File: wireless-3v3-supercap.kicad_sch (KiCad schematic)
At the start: 8 parts

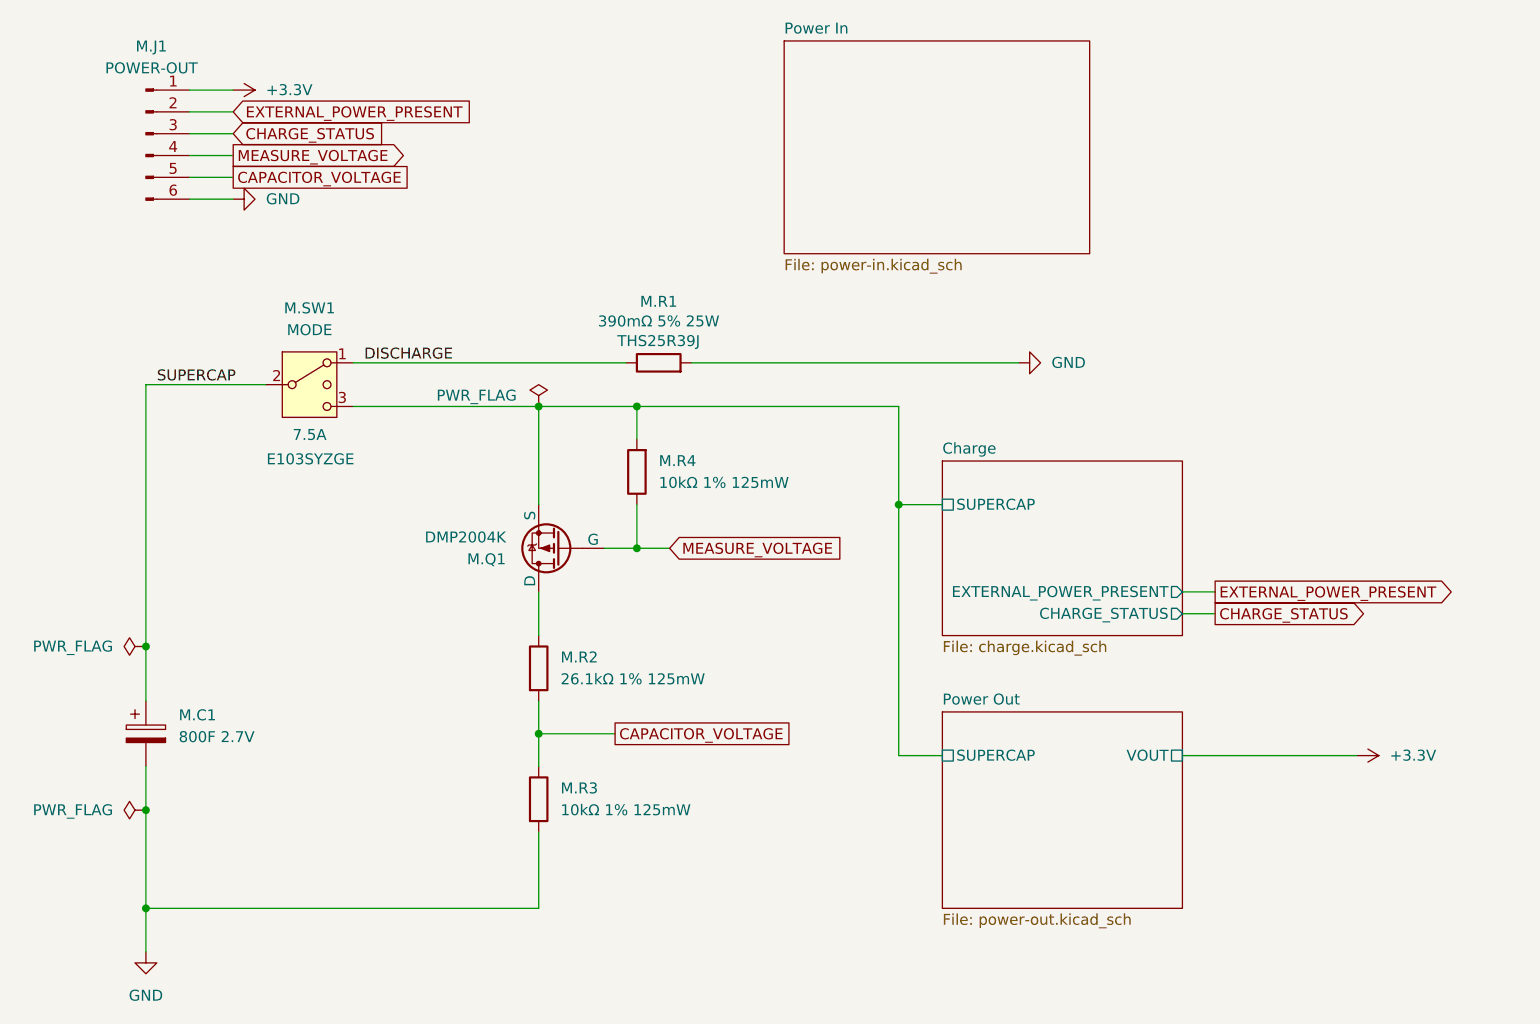
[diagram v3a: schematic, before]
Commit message: Mark signals as active low
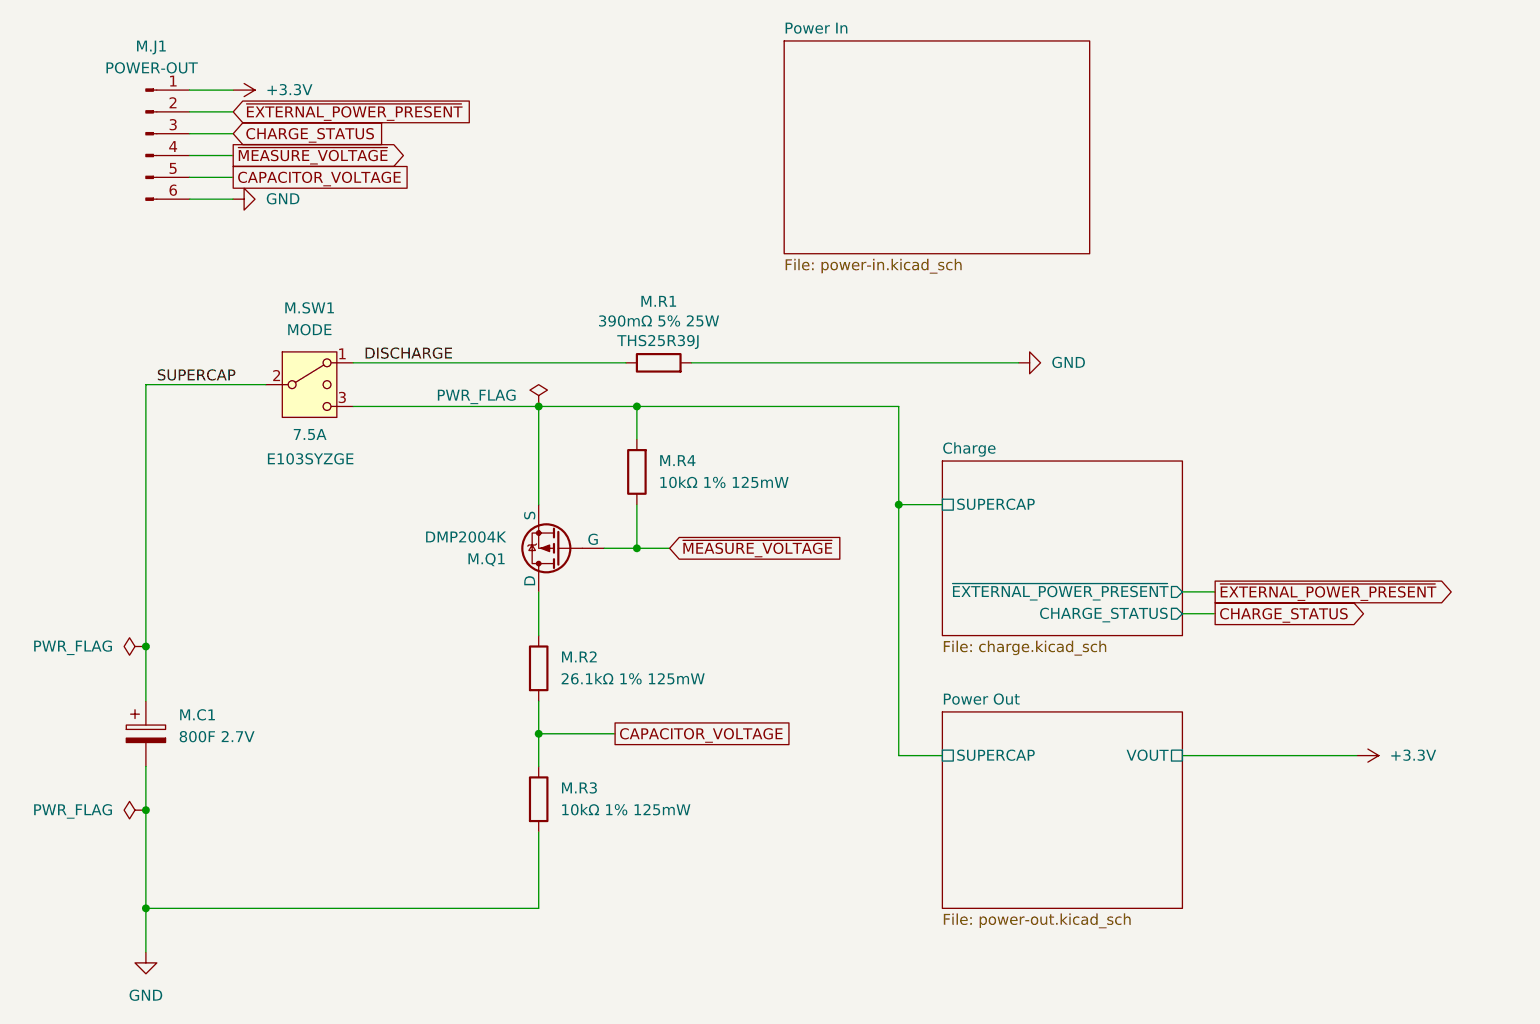
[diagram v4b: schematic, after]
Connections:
- net EXTERNAL_POWER_PRESENT renamed ~{EXTERNAL_POWER_PRESENT}
- net MEASURE_VOLTAGE renamed ~{MEASURE_VOLTAGE}
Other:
- sheet Charge ports: added ~{EXTERNAL_POWER_PRESENT}; removed EXTERNAL_POWER_PRESENT
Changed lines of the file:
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@@
 		)
 	)
-	(global_label "MEASURE_VOLTAGE"
+	(global_label "~{MEASURE_VOLTAGE}"
 		(shape input)
 		(at 86.36 68.58 0)
@@
 		)
 	)
-	(global_label "EXTERNAL_POWER_PRESENT"
+	(global_label "~{EXTERNAL_POWER_PRESENT}"
 		(shape output)
 		(at 149.86 73.66 0)
@@
 		)
 	)
-	(global_label "MEASURE_VOLTAGE"
+	(global_label "~{MEASURE_VOLTAGE}"
 		(shape output)
 		(at 35.56 22.86 0)
@@
 		)
 	)
-	(global_label "EXTERNAL_POWER_PRESENT"
+	(global_label "~{EXTERNAL_POWER_PRESENT}"
 		(shape input)
 		(at 35.56 17.78 0)
@@
 			)
 		)
-		(pin "EXTERNAL_POWER_PRESENT" output
+		(pin "~{EXTERNAL_POWER_PRESENT}" output
 			(at 146.05 73.66 0)
 			(effects

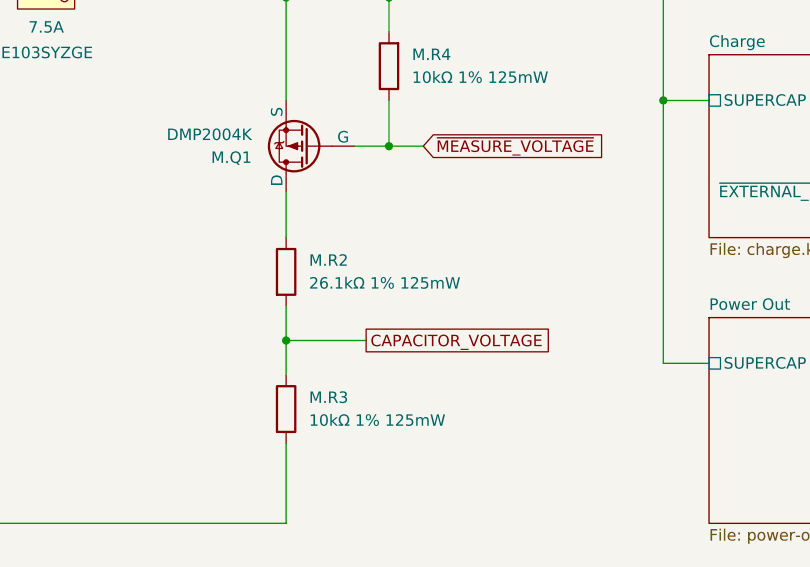
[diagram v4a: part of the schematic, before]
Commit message: Adjust ADC voltage divider
Increase the value of the 0.5V minimum voltage reading to improve accuracy
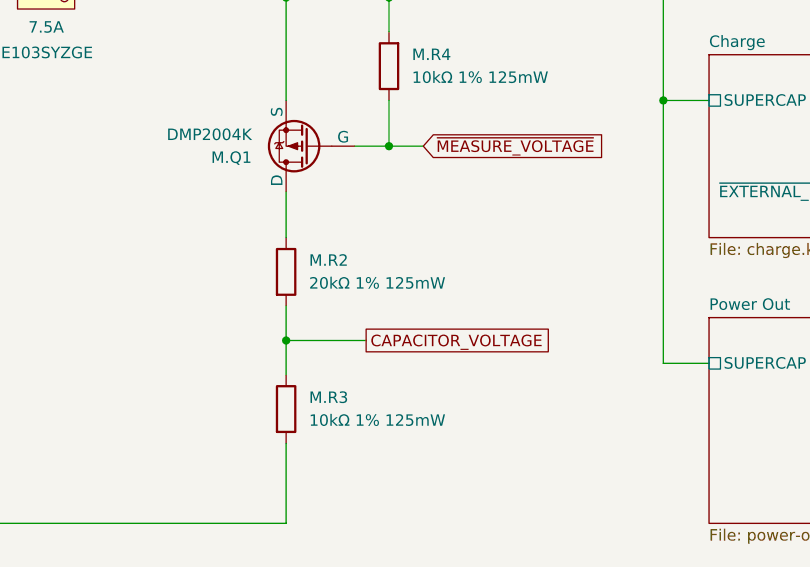
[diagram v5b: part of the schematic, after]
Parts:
- M.R2: value 26.1kΩ 1% 125mW -> 20kΩ 1% 125mW
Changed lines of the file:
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@@
 			)
 		)
-		(property "Value" "26.1kΩ 1% 125mW"
+		(property "Value" "20kΩ 1% 125mW"
 			(at 73.66 83.8199 0)
 			(effects

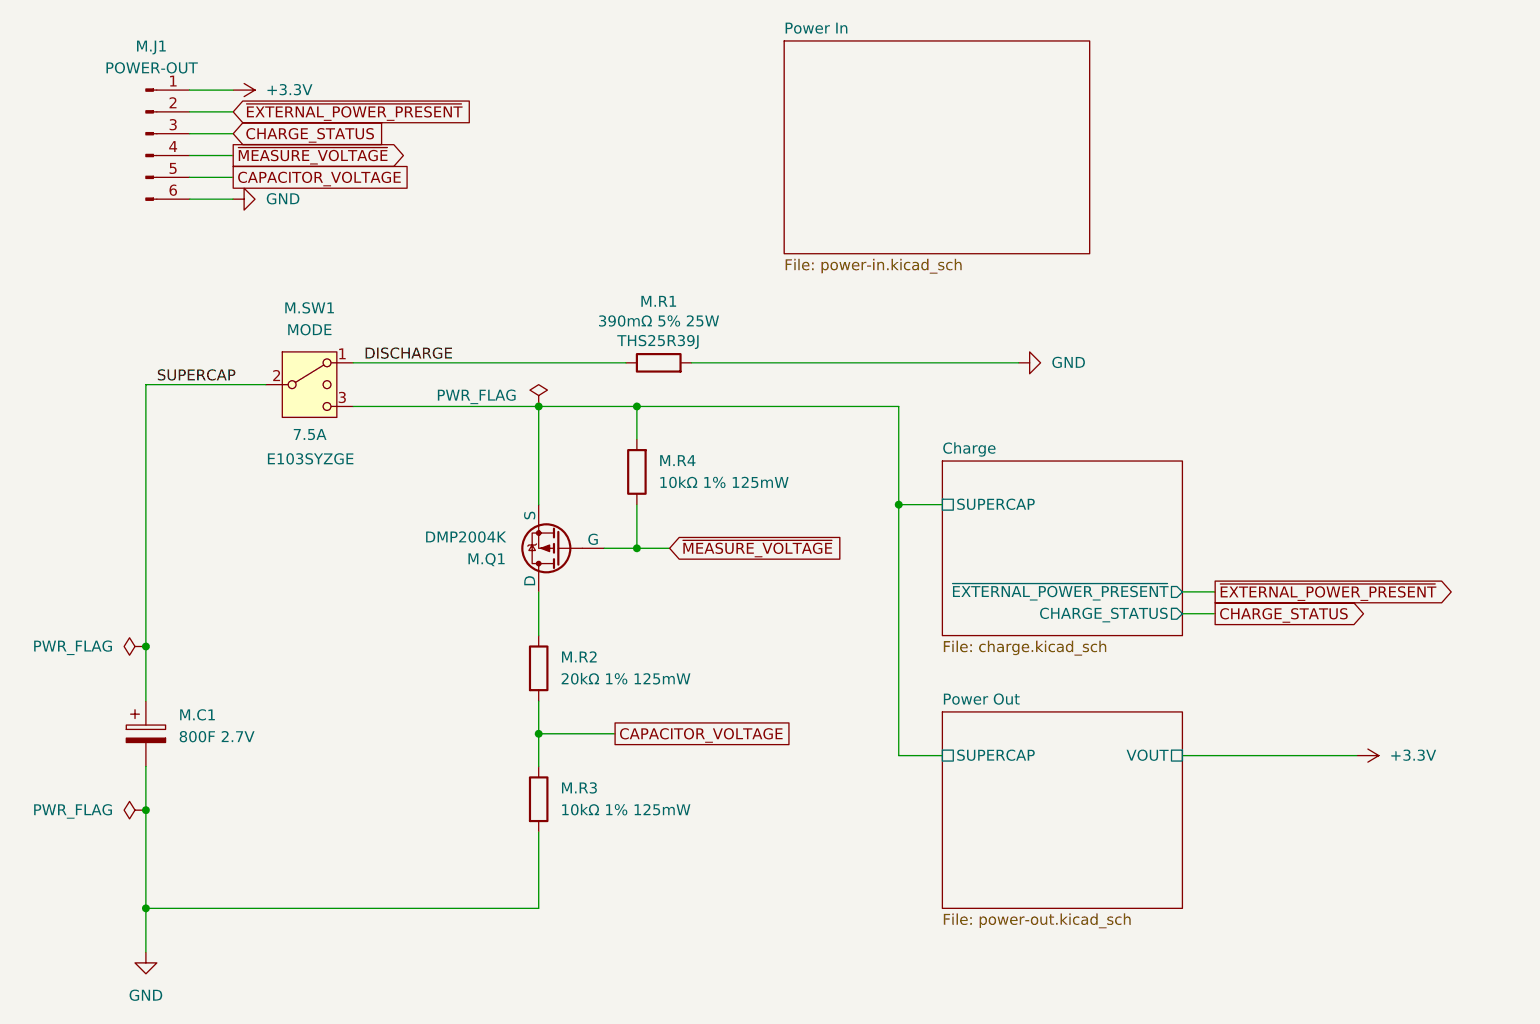
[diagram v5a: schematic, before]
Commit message: Remove voltage divider circuit for ADC
The ESP32-C3 can be configured to handle this directly
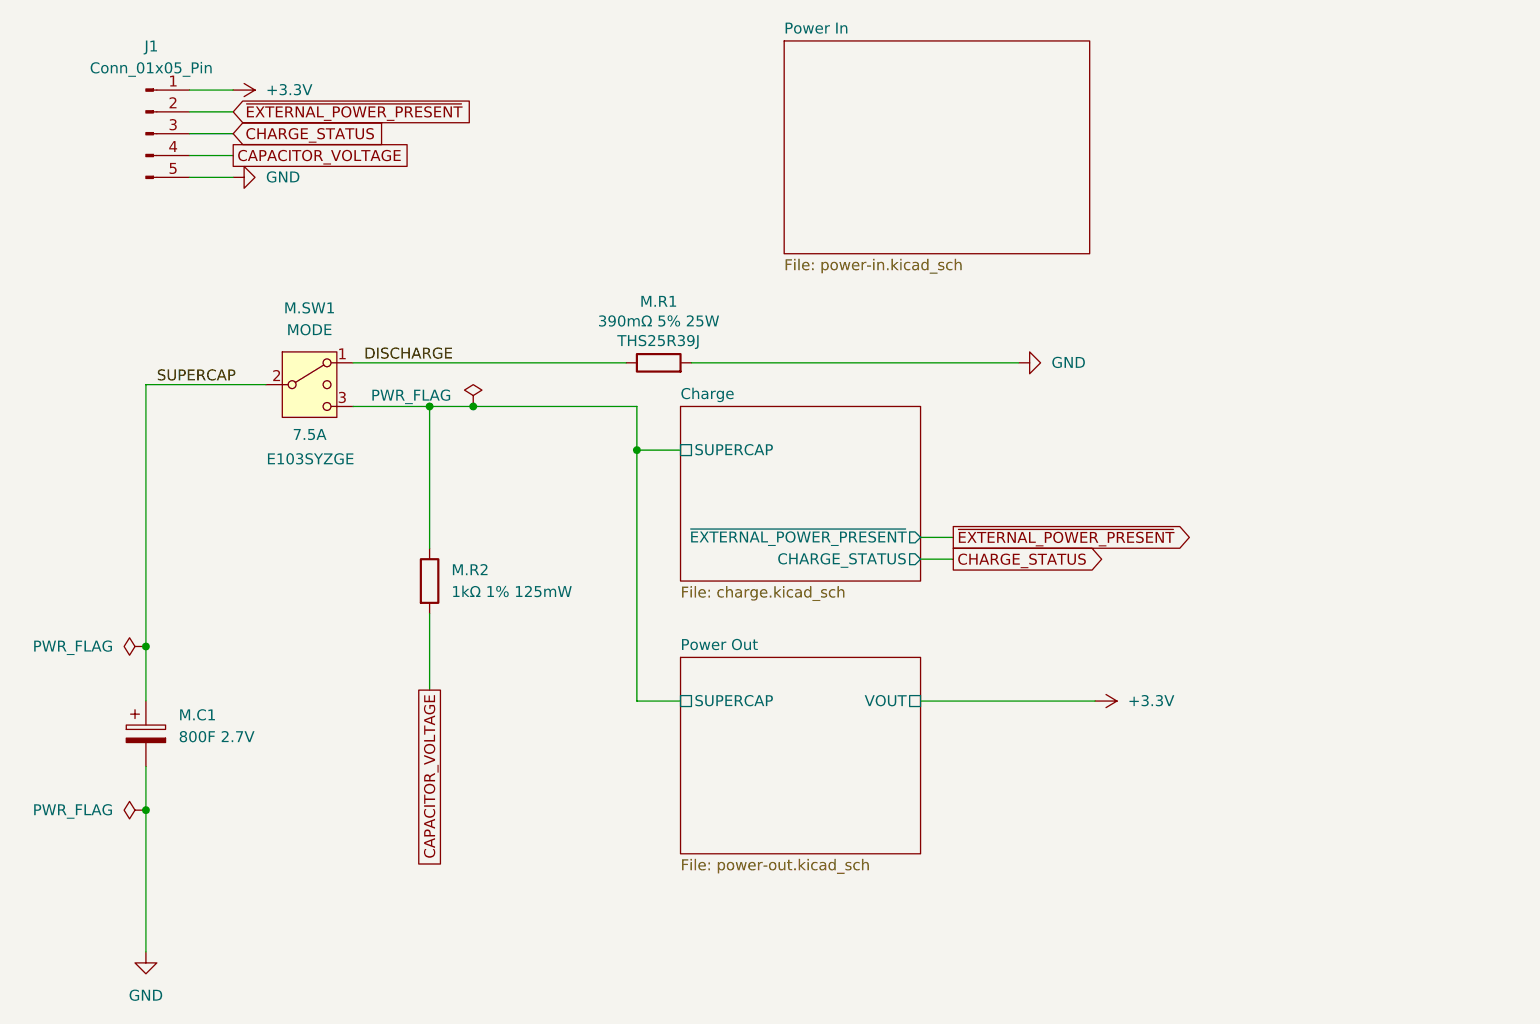
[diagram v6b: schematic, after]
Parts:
- removed M.Q1: DMP2004K, Package_TO_SOT_SMD:SOT-23, symbol Simulation_SPICE:PMOS
- removed M.R3, M.R4: 10kΩ 1% 125mW, Resistor_SMD:R_0805_2012Metric_Pad1.20x1.40mm_HandSolder, symbol Device:R
- J1: renamed from M.J1; value POWER-OUT -> Conn_01x05_Pin; footprint Connector_PinHeader_2.54mm:PinHeader_1x06_P2.54mm_Vertical -> Connector_PinHeader_2.54mm:PinHeader_1x05_P2.54mm_Vertical; symbol Connector:Conn_01x06_Pin -> Connector:Conn_01x05_Pin
- M.R2: value 20kΩ 1% 125mW -> 1kΩ 1% 125mW
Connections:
- net ~{MEASURE_VOLTAGE} is gone; now on net CAPACITOR_VOLTAGE: J1.4 (Pin_4)
- net CAPACITOR_VOLTAGE: no longer J1.5 (Pin_5)
- net Charge/SUPERCAP: now also M.R2.1
- net GND: now also J1.5 (Pin_5); no longer J1.6 (Pin_6)
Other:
- moved on the sheet: M.R2

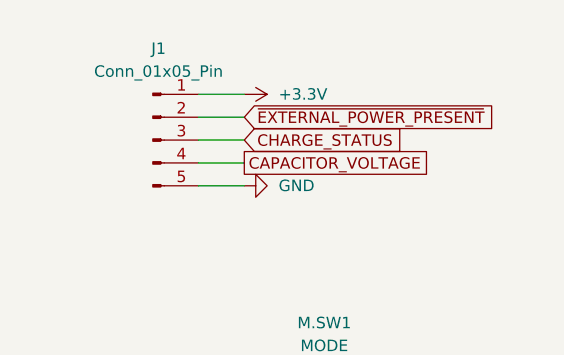
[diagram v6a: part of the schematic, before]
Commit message: Fix pin header name and size
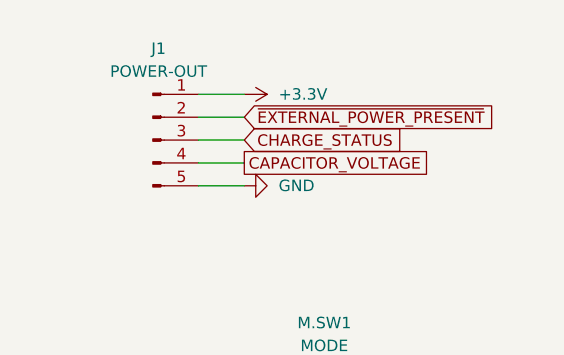
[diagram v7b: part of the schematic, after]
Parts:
- J1: value Conn_01x05_Pin -> POWER-OUT
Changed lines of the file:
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@@
 			)
 		)
-		(property "Value" "Conn_01x05_Pin"
+		(property "Value" "POWER-OUT"
 			(at 26.035 12.7 0)
 			(effects

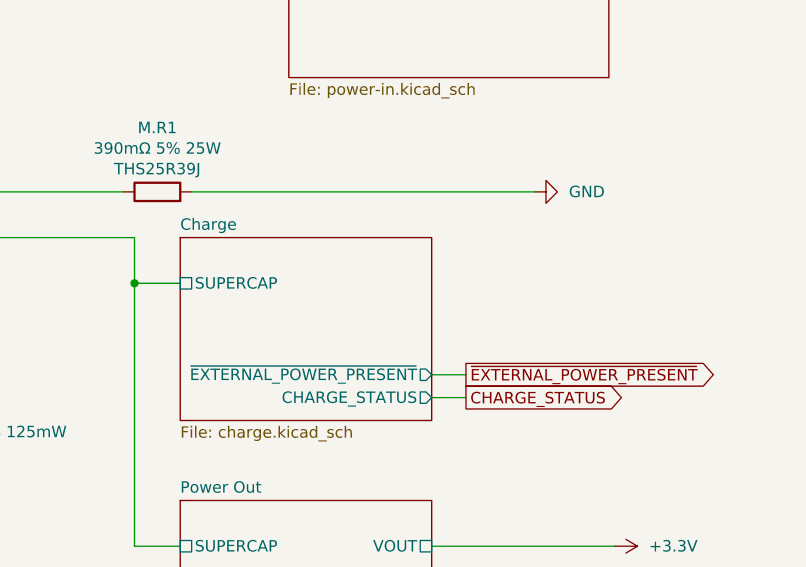
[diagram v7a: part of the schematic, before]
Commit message: Add incomplete charge circuit
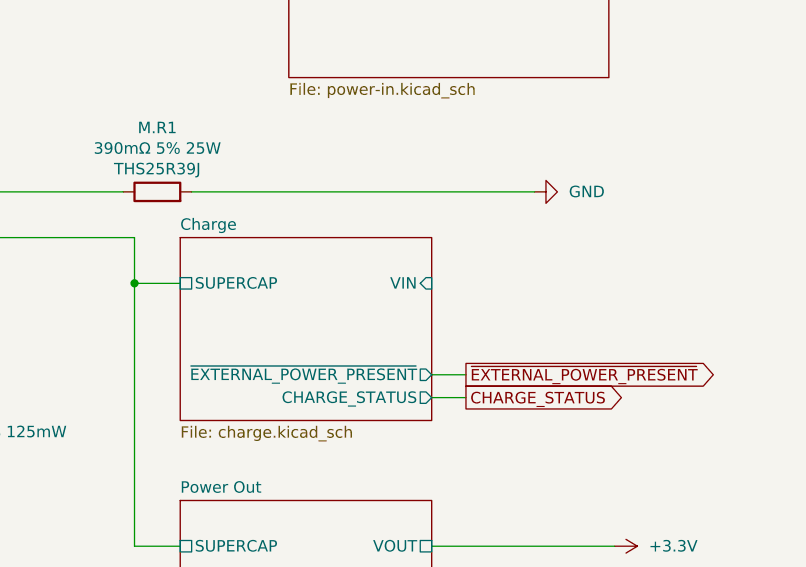
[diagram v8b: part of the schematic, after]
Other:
- sheet Charge ports: added VIN; removed none
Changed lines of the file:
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@@
+			)
+		)
+		(pin "VIN" input
+			(at 115.57 57.15 0)
+			(effects
+				(font
+					(size 1.27 1.27)
+				)
+				(justify right)
 			)
 		)
